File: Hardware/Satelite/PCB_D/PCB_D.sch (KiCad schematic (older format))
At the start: 31 parts, among them J1 Conn_01x03, J2 Conector_Expansion_CanSat, J3 Conn_02x03_Odd_Even, J4 USB_B_Micro, J5 Conn_01x03, M1 Spacer, M2 Spacer, M3 Spacer, SW1 Reset Switch, U1 ATmega328P-AU, U2 CSTNE16M0V530000R0, U3 FT231XS, U4 TPD2E2U06

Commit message: Espaciadores más largos para PCB que usan conector de expansión
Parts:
- M1, M2, M3: Manufacturer Part Number R30-3011002 -> R30-3011202
- U3: symbol PCB_D-rescue:FT231XS-Interface_USB-PCB_D-rescue -> PCB_D-rescue:FT231XS-Interface_USB-PCB_D-rescue-PCB_D-rescue
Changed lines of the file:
@@
 EESchema Schematic File Version 4
 LIBS:PCB_D-cache
-EELAYER 26 0
+EELAYER 29 0
 EELAYER END
 $Descr A4 11693 8268
@@
 F 2 "AXTEC:Empty_Footprint" H 4650 1700 50  0001 C CNN
 F 3 "https://www.mouser.com/datasheet/2/181/R30-301-1135805.pdf" H 4750 1800 50  0001 C CNN
-F 4 "R30-3011002" H 4829 1405 50  0001 L CNN "Manufacturer Part Number"
+F 4 "R30-3011202" H 4829 1405 50  0001 L CNN "Manufacturer Part Number"
 	1    4750 1550
 	1    0    0    -1
@@
 F 2 "AXTEC:Empty_Footprint" H 5200 1700 50  0001 C CNN
 F 3 "https://www.mouser.com/datasheet/2/181/R30-301-1135805.pdf" H 5300 1800 50  0001 C CNN
-F 4 "R30-3011002" H 5379 1405 50  0001 L CNN "Manufacturer Part Number"
+F 4 "R30-3011202" H 5379 1405 50  0001 L CNN "Manufacturer Part Number"
 	1    5300 1550
 	1    0    0    -1
@@
 F 2 "AXTEC:Empty_Footprint" H 5750 1700 50  0001 C CNN
 F 3 "https://www.mouser.com/datasheet/2/181/R30-301-1135805.pdf" H 5850 1800 50  0001 C CNN
-F 4 "R30-3011002" H 5929 1405 50  0001 L CNN "Manufacturer Part Number"
+F 4 "R30-3011202" H 5929 1405 50  0001 L CNN "Manufacturer Part Number"
 	1    5850 1550
 	1    0    0    -1
@@
 	9750 2800 9850 2800
 $Comp
-L PCB_D-rescue:FT231XS-Interface_USB-PCB_D-rescue U3
+L PCB_D-rescue:FT231XS-Interface_USB-PCB_D-rescue-PCB_D-rescue U3
 U 1 1 5C33DAA5
 P 8750 3000

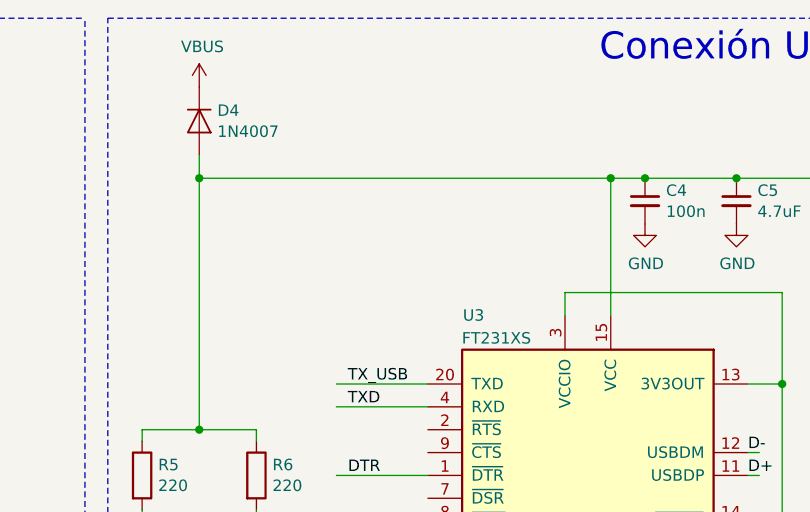
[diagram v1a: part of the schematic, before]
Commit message: PCB_D:
- Corregidas librerías
- Agregado diodo para poder alimentar el Arduino tanto cuando esta solo como cuando se encuentra en el stack del CanSat
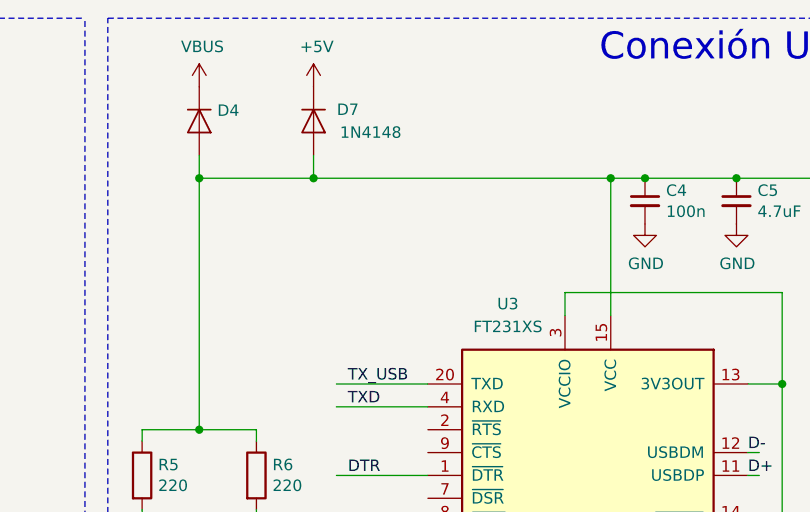
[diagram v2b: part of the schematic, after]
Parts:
- removed U3: FT231XS, Package_SO:SSOP-20_3.9x8.7mm_P0.635mm, symbol PCB_D-rescue:FT231XS-Interface_USB-PCB_D-rescue-PCB_D-rescue
- added D7: 1N4148, Diode_SMD:D_MiniMELF, symbol Diode:1N4148
- added U3: FT231XS, Package_SO:SSOP-20_3.9x8.7mm_P0.635mm, symbol Interface_USB:FT231XS
- D4: value 1N4007 -> RS1A-E3/5AT; Manufacturer Part Number (none) -> RS1A-E3/5AT
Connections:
- wire segments 155 -> 157
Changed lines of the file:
@@
 	1700 1450 1800 1450
 Wire Wire Line
-	7050 1500 8850 1500
+	7050 1500 7550 1500
 $Comp
 L AXTEC_IC:Spacer M1
@@
 Wire Wire Line
 	3100 1400 3450 1400
-$Comp
-L Diode:1N4007 D4
-U 1 1 5C28CCE7
-P 7050 1250
-F 0 "D4" V 7004 1329 50  0000 L CNN
-F 1 "1N4007" V 7096 1329 50  0000 L CNN
-F 2 "Diode_SMD:D_SMA" H 7050 1075 50  0001 C CNN
-F 3 "http://www.vishay.com/docs/88503/1n4001.pdf" H 7050 1250 50  0001 C CNN
-	1    7050 1250
-	0    1    1    0
-$EndComp
 Text Label 3150 2100 0    50   ~ 0
 D6
@@
 D+
 $Comp
-L Graphic:Logo_Open_Hardware_Large #LOGO?
+L Graphic:Logo_Open_Hardware_Large #LOGO1
 U 1 1 5C3319FC
 P 8750 5500
-F 0 "#LOGO?" H 8750 6000 50  0001 C CNN
+F 0 "#LOGO1" H 8750 6000 50  0001 C CNN
 F 1 "Logo_Open_Hardware_Large" H 8750 5100 50  0001 C CNN
 F 2 "" H 8750 5500 50  0001 C CNN
@@
 	9750 2800 9850 2800
 $Comp
-L PCB_D-rescue:FT231XS-Interface_USB-PCB_D-rescue-PCB_D-rescue U3
-U 1 1 5C33DAA5
-P 8750 3000
-F 0 "U3" H 9250 3900 50  0000 C CNN
-F 1 "FT231XS" H 9150 3800 50  0000 C CNN
-F 2 "Package_SO:SSOP-20_3.9x8.7mm_P0.635mm" H 9350 2050 50  0001 C CNN
-F 3 "http://www.ftdichip.com/Products/ICs/FT231X.html" H 8750 3000 50  0001 C CNN
-	1    8750 3000
-	-1   0    0    -1
-$EndComp
-$Comp
-L power:GND #PWR?
+L power:GND #PWR024
 U 1 1 5C73E497
 P 7900 3750
-F 0 "#PWR?" H 7900 3500 50  0001 C CNN
+F 0 "#PWR024" H 7900 3500 50  0001 C CNN
 F 1 "GND" H 7904 3576 50  0000 C CNN
 F 2 "" H 7900 3750 50  0001 C CNN
@@
 Wire Wire Line
 	7900 3600 7900 3750
+$Comp
+L Interface_USB:FT231XS U3
+U 1 1 5CD17CE6
+P 8750 3000
+F 0 "U3" H 9100 3950 50  0000 C CNN
+F 1 "FT231XS" H 9100 3850 50  0000 C CNN
+F 2 "Package_SO:SSOP-20_3.9x8.7mm_P0.635mm" H 9350 2050 50  0001 C CNN
+F 3 "http://www.ftdichip.com/Products/ICs/FT231X.html" H 8750 3000 50  0001 C CNN
+F 4 "FT231XS-U" H 8750 3000 50  0001 C CNN "Manufacturer Part Number"
+	1    8750 3000
+	-1   0    0    -1
+$EndComp
+Wire Wire Line
+	7550 1400 7550 1500
+Connection ~ 7550 1500
+Wire Wire Line
+	7550 1500 8850 1500
+$Comp
+L power:+5V #PWR023
+U 1 1 5CD2C70A
+P 7550 1100
+F 0 "#PWR023" H 7550 950 50  0001 C CNN
+F 1 "+5V" H 7564 1275 50  0000 C CNN
+F 2 "" H 7550 1100 50  0001 C CNN
+F 3 "" H 7550 1100 50  0001 C CNN
+	1    7550 1100
+	1    0    0    -1
+$EndComp
+$Comp
+L Diode:1N4007 D4
+U 1 1 5C28CCE7
+P 7050 1250
+F 0 "D4" V 7004 1329 50  0000 L CNN
+F 1 "RS1A-E3/5AT" V 7096 1329 50  0001 L CNN
+F 2 "Diode_SMD:D_SMA" H 7050 1075 50  0001 C CNN
+F 3 "http://www.vishay.com/docs/88503/1n4001.pdf" H 7050 1250 50  0001 C CNN
+F 4 "RS1A-E3/5AT" V 7050 1250 50  0001 C CNN "Manufacturer Part Number"
+	1    7050 1250
+	0    1    1    0
+$EndComp
+$Comp
+L Diode:1N4148 D7
+U 1 1 5CD16F3E
+P 7550 1250
+F 0 "D7" V 7500 1400 50  0000 C CNN
+F 1 "1N4148" V 7600 1500 50  0000 C CNN
+F 2 "Diode_SMD:D_MiniMELF" H 7550 1075 50  0001 C CNN
+F 3 "https://www.vishay.com/docs/85561/ls4148.pdf" H 7550 1250 50  0001 C CNN
+F 4 "LS4148-GS08" H 7550 1250 50  0001 C CNN "Manufacturer Part Number"
+	1    7550 1250
+	0    1    1    0
+$EndComp
 $EndSCHEMATC

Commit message: Nuevos conectores micro-usb completamente SMD
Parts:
- J4: footprint Connector_USB:USB_Micro-B_Molex-105017-0001 -> Connector_USB:USB_Micro-B_Molex_47346-0001; Manufacturer Part Number 105017-0001 -> 47346-1001
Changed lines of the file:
@@
 F 0 "J4" H 9920 2691 50  0000 R CNN
 F 1 "USB_B_Micro" H 9920 2599 50  0000 R CNN
-F 2 "Connector_USB:USB_Micro-B_Molex-105017-0001" H 10300 2650 50  0001 C CNN
+F 2 "Connector_USB:USB_Micro-B_Molex_47346-0001" H 10300 2650 50  0001 C CNN
 F 3 "https://www.molex.com/pdm_docs/sd/1050170001_sd.pdf" H 10300 2650 50  0001 C CNN
-F 4 "105017-0001" H 10150 2700 50  0001 C CNN "Manufacturer Part Number"
+F 4 "47346-1001" H 10150 2700 50  0001 C CNN "Manufacturer Part Number"
 	1    10150 2700
 	-1   0    0    -1

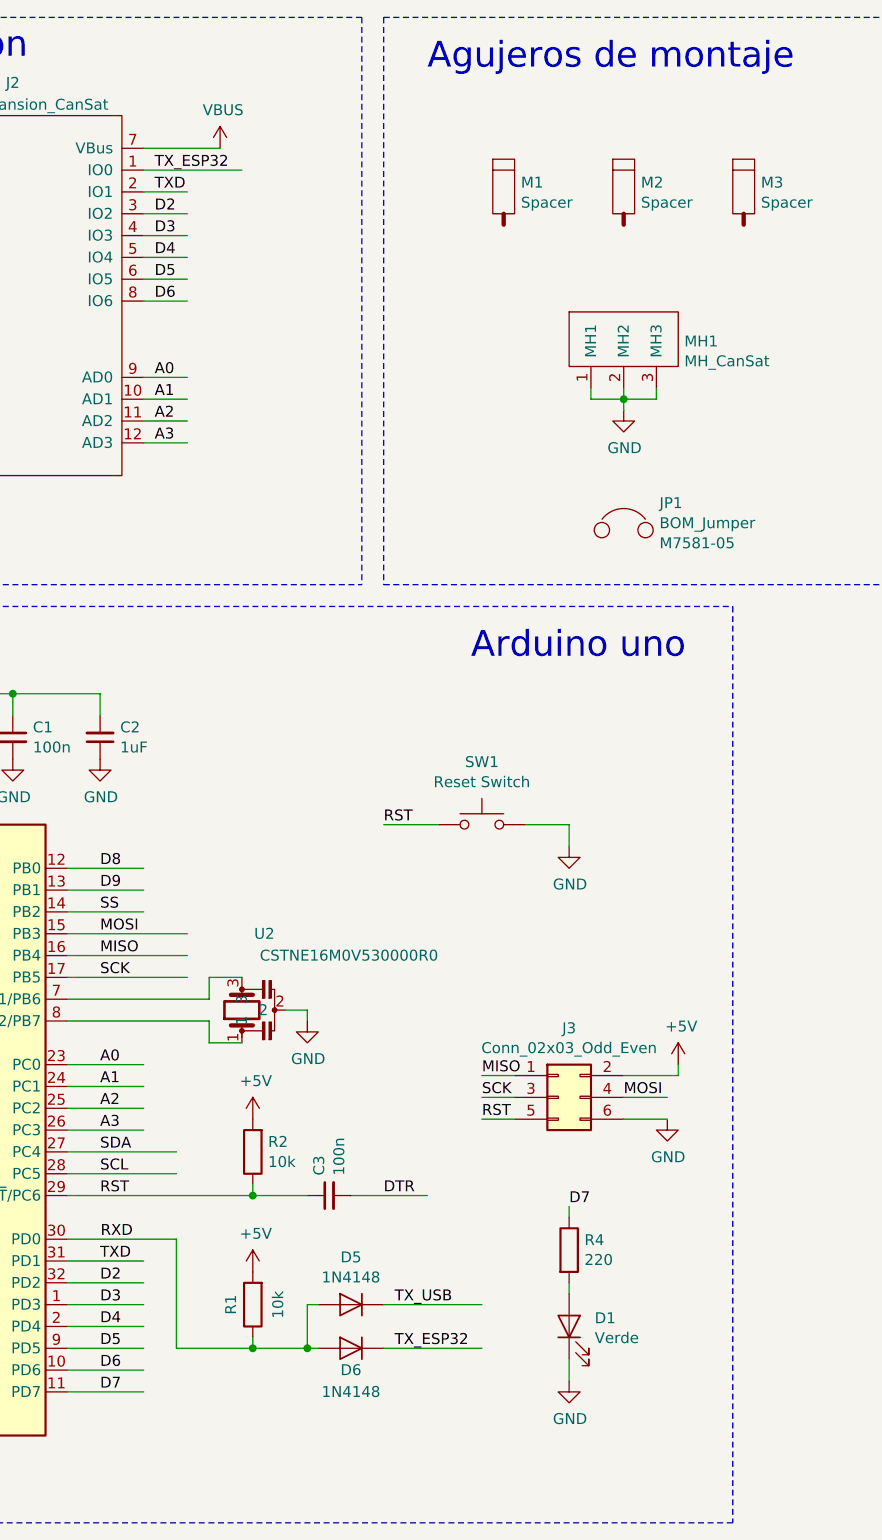
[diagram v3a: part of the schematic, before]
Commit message: Agregado transistor para led en SCK PCB_D + correcciones de silkscreen
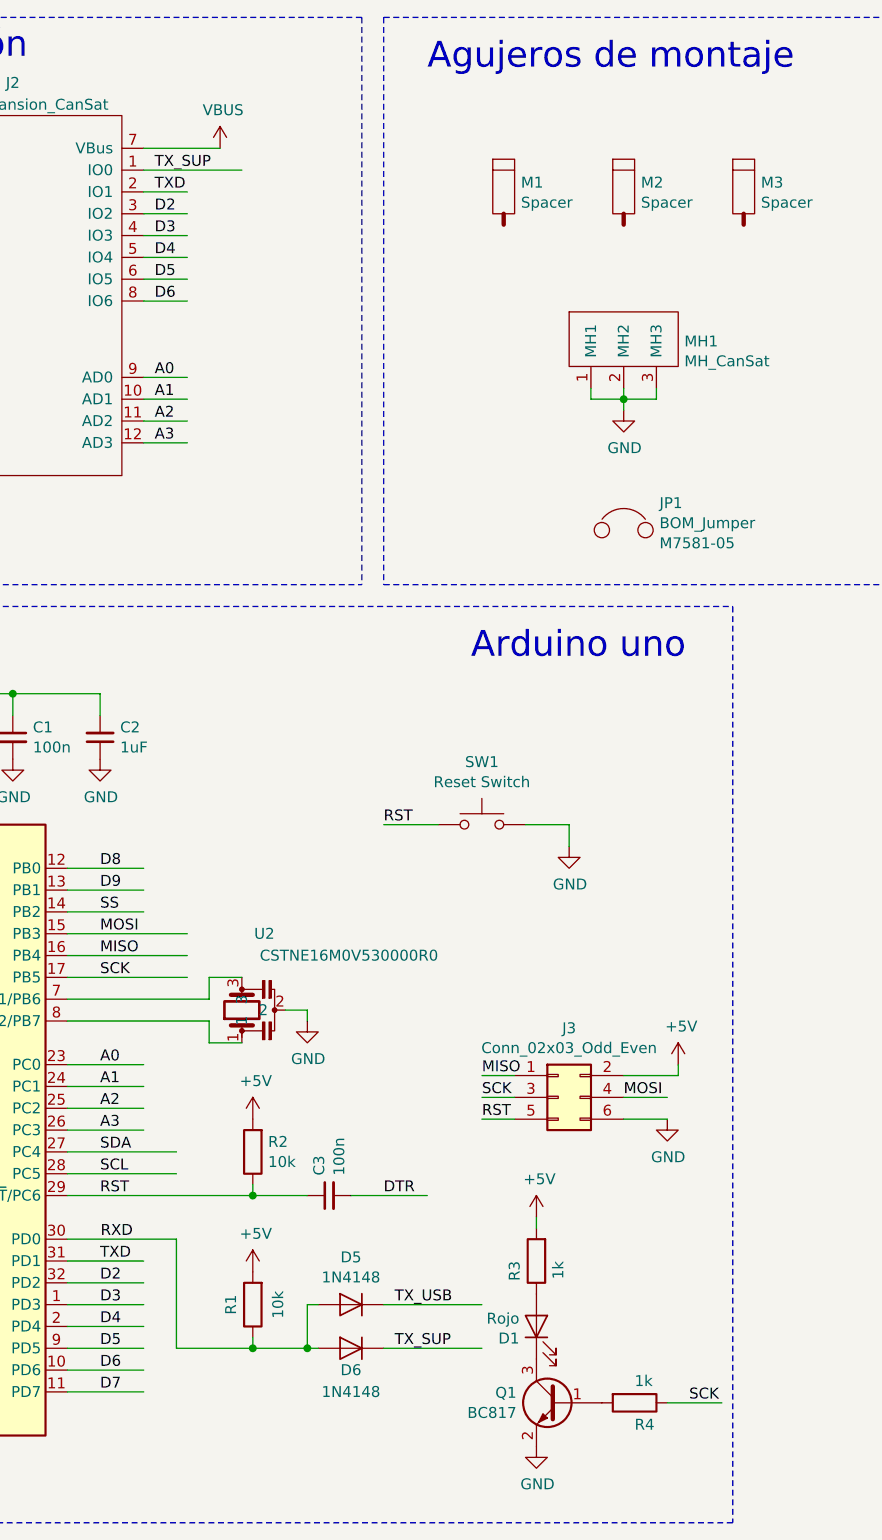
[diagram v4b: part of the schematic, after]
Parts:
- added Q1: BC817, Package_TO_SOT_SMD:SOT-23, symbol Transistor_BJT:BC817
- added R3: 1k, Resistor_SMD:R_0603_1608Metric_Pad1.05x0.95mm_HandSolder, symbol Device:R
- D1: value Verde -> Rojo; footprint LED_SMD:LED_0603_1608Metric -> LED_SMD:LED_0603_1608Metric_Pad1.05x0.95mm_HandSolder; Manufacturer Part Number 150060VS75000 -> 150060RS75000
- R4: value 220 -> 1k; Manufacturer Part Number RC0603JR-13220RL -> RC0603JR-071KL
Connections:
- net labels added: TX_SUP
- net labels removed: TX_ESP32
- wire segments 157 -> 156
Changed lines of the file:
@@
 	2500 3900 2900 3900
 Connection ~ 2150 3900
-Text Label 5050 6250 0    50   ~ 0
-D7
 Text Label 3150 1700 0    50   ~ 0
 D2
@@
 	7050 1500 7050 2600
 Connection ~ 8850 1500
-Wire Wire Line
-	5050 6250 5050 6300
-$Comp
-L Device:LED D?
-U 1 1 5BC9091B
-P 5050 6800
-AR Path="/5B9997DB/5BC9091B" Ref="D?"  Part="1"
-AR Path="/5BC9091B" Ref="D1"  Part="1"
-F 0 "D1" V 5088 6683 50  0000 R CNN
-F 1 "Verde" V 4997 6683 50  0000 R CNN
-F 2 "LED_SMD:LED_0603_1608Metric" H 5050 6800 50  0001 C CNN
-F 3 "~" H 5050 6800 50  0001 C CNN
-F 4 "150060VS75000" V 5050 6800 50  0001 C CNN "Manufacturer Part Number"
-	1    5050 6800
-	0    -1   -1   0
-$EndComp
-Wire Wire Line
-	5050 6650 5050 6600
-$Comp
-L power:GND #PWR013
-U 1 1 5BC96C3C
-P 5050 7050
-F 0 "#PWR013" H 5050 6800 50  0001 C CNN
-F 1 "GND" H 5054 6876 50  0000 C CNN
-F 2 "" H 5050 7050 50  0001 C CNN
-F 3 "" H 5050 7050 50  0001 C CNN
-	1    5050 7050
-	1    0    0    -1
-$EndComp
-Wire Wire Line
-	5050 7050 5050 6950
 $Comp
 L Connector_Generic:Conn_01x03 J1
@@
 $EndComp
 $Comp
-L Device:R R?
-U 1 1 5C2EDFB7
-P 5050 6450
-AR Path="/5B9997DB/5C2EDFB7" Ref="R?"  Part="1"
-AR Path="/5C2EDFB7" Ref="R4"  Part="1"
-F 0 "R4" H 5120 6496 50  0000 L CNN
-F 1 "220" H 5120 6405 50  0000 L CNN
-F 2 "Resistor_SMD:R_0603_1608Metric_Pad1.05x0.95mm_HandSolder" V 4980 6450 50  0001 C CNN
-F 3 "~" H 5050 6450 50  0001 C CNN
-F 4 "RC0603JR-13220RL" H 5050 6450 50  0001 C CNN "Manufacturer Part Number"
-	1    5050 6450
-	1    0    0    -1
-$EndComp
-$Comp
 L AXTEC_IC:BOM_Jumper JP1
 U 1 1 5C31B4FD
@@
 TXD
 Text Label 3150 1500 0    50   ~ 0
-TX_ESP32
+TX_SUP
 Text Label 1200 5400 2    50   ~ 0
 RXD
@@
 Text Label 4250 6700 0    50   ~ 0
 TX_USB
-Text Label 4250 6900 0    50   ~ 0
-TX_ESP32
 Wire Wire Line
 	4200 6900 4650 6900
@@
 	0    1    1    0
 $EndComp
+$Comp
+L Device:R R?
+U 1 1 5CDE5E1F
+P 4900 6500
+AR Path="/5BA17F9C/5CDE5E1F" Ref="R?"  Part="1"
+AR Path="/5BA1A7F9/5CDE5E1F" Ref="R?"  Part="1"
+AR Path="/5BA1A77A/5CDE5E1F" Ref="R?"  Part="1"
+AR Path="/5CDE5E1F" Ref="R3"  Part="1"
+F 0 "R3" V 5000 6500 50  0000 L CNN
+F 1 "1k" V 4800 6500 50  0000 L CNN
+F 2 "Resistor_SMD:R_0603_1608Metric_Pad1.05x0.95mm_HandSolder" V 4830 6500 50  0001 C CNN
+F 3 "~" H 4900 6500 50  0001 C CNN
+F 4 "RC0603JR-071KL" V 4900 6500 50  0001 C CNN "Manufacturer Part Number"
+	1    4900 6500
+	-1   0    0    1
+$EndComp
+$Comp
+L power:GND #PWR025
+U 1 1 5CDE5E2B
+P 4900 7350
+F 0 "#PWR025" H 4900 7100 50  0001 C CNN
+F 1 "GND" H 4905 7177 50  0000 C CNN
+F 2 "" H 4900 7350 50  0001 C CNN
+F 3 "" H 4900 7350 50  0001 C CNN
+	1    4900 7350
+	1    0    0    -1
+$EndComp
+$Comp
+L Transistor_BJT:BC817 Q1
+U 1 1 5CDE5E32
+P 5000 7150
+F 0 "Q1" H 5191 7196 50  0000 L CNN
+F 1 "BC817" H 5191 7104 50  0000 L CNN
+F 2 "Package_TO_SOT_SMD:SOT-23" H 5200 7075 50  0001 L CIN
+F 3 "http://www.fairchildsemi.com/ds/BC/BC817.pdf" H 5000 7150 50  0001 L CNN
+F 4 "BC817-16LT1G" H 5000 7150 50  0001 C CNN "Manufacturer Part Number"
+	1    5000 7150
+	-1   0    0    -1
+$EndComp
+Wire Wire Line
+	5500 7150 5750 7150
+$Comp
+L Device:R R?
+U 1 1 5CDE5E3B
+P 5350 7150
+AR Path="/5BA17F9C/5CDE5E3B" Ref="R?"  Part="1"
+AR Path="/5BA1A7F9/5CDE5E3B" Ref="R?"  Part="1"
+AR Path="/5BA1A77A/5CDE5E3B" Ref="R?"  Part="1"
+AR Path="/5CDE5E3B" Ref="R4"  Part="1"
+F 0 "R4" V 5450 7150 50  0000 L CNN
+F 1 "1k" V 5250 7150 50  0000 L CNN
+F 2 "Resistor_SMD:R_0603_1608Metric_Pad1.05x0.95mm_HandSolder" V 5280 7150 50  0001 C CNN
+F 3 "~" H 5350 7150 50  0001 C CNN
+F 4 "RC0603JR-071KL" V 5350 7150 50  0001 C CNN "Manufacturer Part Number"
+	1    5350 7150
+	0    1    1    0
+$EndComp
+$Comp
+L Device:LED D1
+U 1 1 5CDE5E42
+P 4900 6800
+F 0 "D1" V 4845 6878 50  0000 L CNN
+F 1 "Rojo" V 4936 6878 50  0000 L CNN
+F 2 "LED_SMD:LED_0603_1608Metric_Pad1.05x0.95mm_HandSolder" H 4900 6800 50  0001 C CNN
+F 3 "~" H 4900 6800 50  0001 C CNN
+F 4 "150060RS75000" V 4900 6800 50  0001 C CNN "Manufacturer Part Number"
+	1    4900 6800
+	0    -1   -1   0
+$EndComp
+$Comp
+L power:+5V #PWR013
+U 1 1 5CDED934
+P 4900 6300
+F 0 "#PWR013" H 4900 6150 50  0001 C CNN
+F 1 "+5V" H 4914 6475 50  0000 C CNN
+F 2 "" H 4900 6300 50  0001 C CNN
+F 3 "" H 4900 6300 50  0001 C CNN
+	1    4900 6300
+	1    0    0    -1
+$EndComp
+Wire Wire Line
+	4900 6300 4900 6350
+Text Label 5600 7150 0    50   ~ 0
+SCK
+Text Label 4250 6900 0    50   ~ 0
+TX_SUP
 $EndSCHEMATC
